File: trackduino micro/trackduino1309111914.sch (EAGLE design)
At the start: 35 parts, among them IC1 74AHC1G125DBV, IC2 74AHC1G125DBV, IC3 74AHC1G125DBV, U1 ATMEGA168

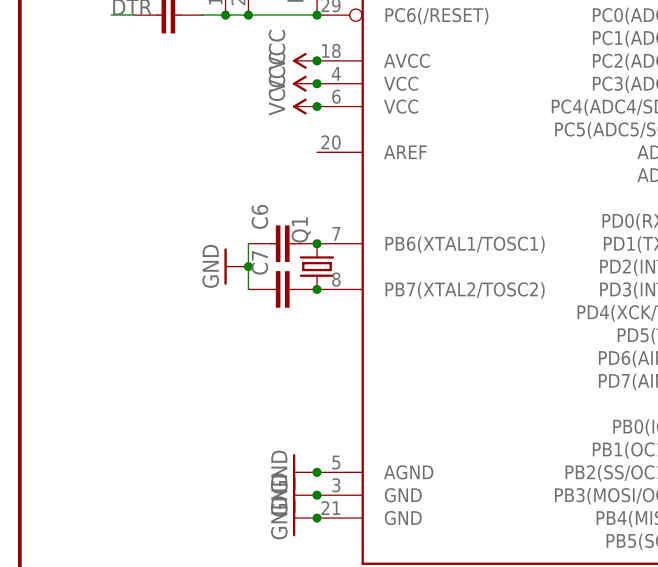
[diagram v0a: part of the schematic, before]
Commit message: swapped crystal for smaller resonator
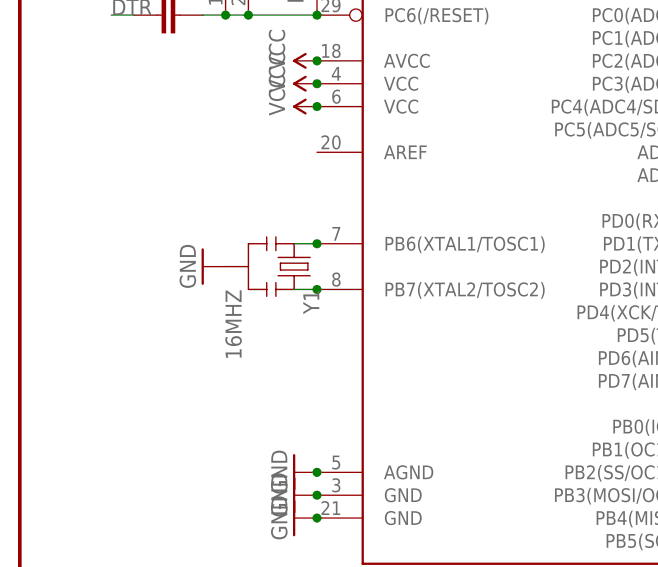
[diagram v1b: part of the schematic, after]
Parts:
- removed C6, C7: (no value), SparkFun-Capacitors:CAP0805
- removed Q1: (no value), crystal:CRYSTALCTS406
- added Y1: 16MHZ, SparkFun-FreqCtrl:RESONATOR16MHZ
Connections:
- net GND: now also Y1.2; no longer C6.1, C7.1
- net N$14: now also U1.PB7(XTAL2/TOSC2), Y1.3; no longer C6.2, Q1.2, U1.PB6(XTAL1/TOSC1)
- net N$26: now also U1.PB6(XTAL1/TOSC1), Y1.1; no longer C7.2, Q1.1, U1.PB7(XTAL2/TOSC2)
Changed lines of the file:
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@@
 <part name="S1" library="SparkFun-Electromechanical" deviceset="TAC_SWITCH" device="SMD" value="TAC_SWITCHSMD"/>
 <part name="GND23" library="SparkFun-Aesthetics" deviceset="GND" device=""/>
-<part name="Q1" library="crystal" deviceset="CRYSTAL" device="CTS406"/>
-<part name="C6" library="SparkFun-Capacitors" deviceset="CAP" device="0805"/>
-<part name="C7" library="SparkFun-Capacitors" deviceset="CAP" device="0805"/>
-<part name="GND24" library="SparkFun-Aesthetics" deviceset="GND" device=""/>
 <part name="FRAME1" library="SparkFun-Aesthetics" deviceset="FRAME-LETTER" device=""/>
 <part name="SUPPLY11" library="SparkFun-Aesthetics" deviceset="VCC" device=""/>
@@
 <part name="R6" library="SparkFun-Resistors" deviceset="RESISTOR" device="0805-RES"/>
 <part name="GND26" library="SparkFun-Aesthetics" deviceset="GND" device=""/>
+<part name="GND24" library="SparkFun-Aesthetics" deviceset="GND" device=""/>
+<part name="Y1" library="SparkFun-FreqCtrl" deviceset="RESONATOR" device="16MHZ" value="16MHZ"/>
 </parts>
 <sheets>
@@
 <instance part="S1" gate="S" x="22.86" y="86.36" rot="R90"/>
 <instance part="GND23" gate="1" x="27.94" y="91.44" rot="R90"/>
-<instance part="Q1" gate="G$1" x="33.02" y="53.34" rot="R90"/>
-<instance part="C6" gate="G$1" x="30.48" y="55.88" rot="R90"/>
-<instance part="C7" gate="G$1" x="30.48" y="50.8" rot="R90"/>
-<instance part="GND24" gate="1" x="22.86" y="53.34" rot="R270"/>
 <instance part="FRAME1" gate="G$1" x="0" y="0"/>
 <instance part="FRAME1" gate="G$2" x="147.32" y="0"/>
@@
 <instance part="R6" gate="G$1" x="154.94" y="68.58" rot="R270"/>
 <instance part="GND26" gate="1" x="154.94" y="83.82" rot="R180"/>
+<instance part="GND24" gate="1" x="20.32" y="53.34" rot="R270"/>
+<instance part="Y1" gate="G$1" x="30.48" y="53.34" rot="R270"/>
 </instances>
 <busses>
@@
 </segment>
 <segment>
-<pinref part="C6" gate="G$1" pin="1"/>
-<pinref part="C7" gate="G$1" pin="1"/>
-<wire x1="25.4" y1="55.88" x2="25.4" y2="53.34" width="0.1524" layer="91"/>
-<pinref part="GND24" gate="1" pin="GND"/>
-<wire x1="25.4" y1="53.34" x2="25.4" y2="50.8" width="0.1524" layer="91"/>
-<junction x="25.4" y="53.34"/>
-</segment>
-<segment>
 <pinref part="U1" gate="G$1" pin="AGND"/>
 <pinref part="GND25" gate="1" pin="GND"/>
@@
 <pinref part="GND26" gate="1" pin="GND"/>
 <junction x="154.94" y="81.28"/>
+</segment>
+<segment>
+<pinref part="GND24" gate="1" pin="GND"/>
+<pinref part="Y1" gate="G$1" pin="2"/>
 </segment>
 </net>
@@
 </segment>
 </net>
-<net name="N$14" class="0">
-<segment>
-<pinref part="U1" gate="G$1" pin="PB6(XTAL1/TOSC1)"/>
-<pinref part="Q1" gate="G$1" pin="2"/>
-<pinref part="C6" gate="G$1" pin="2"/>
-<junction x="33.02" y="55.88"/>
-<pinref part="C6" gate="G$1" pin="2"/>
-</segment>
-</net>
-<net name="N$26" class="0">
-<segment>
-<pinref part="U1" gate="G$1" pin="PB7(XTAL2/TOSC2)"/>
-<pinref part="Q1" gate="G$1" pin="1"/>
-<pinref part="C7" gate="G$1" pin="2"/>
-<junction x="33.02" y="50.8"/>
-<pinref part="C7" gate="G$1" pin="2"/>
-</segment>
-</net>
 <net name="N$27" class="0">
 <segment>
@@
 </segment>
 </net>
+<net name="N$14" class="0">
+<segment>
+<pinref part="U1" gate="G$1" pin="PB7(XTAL2/TOSC2)"/>
+<wire x1="30.48" y1="50.8" x2="33.02" y2="50.8" width="0.1524" layer="91"/>
+<junction x="33.02" y="50.8"/>
+<pinref part="Y1" gate="G$1" pin="3"/>
+</segment>
+</net>
+<net name="N$26" class="0">
+<segment>
+<pinref part="U1" gate="G$1" pin="PB6(XTAL1/TOSC1)"/>
+<wire x1="30.48" y1="55.88" x2="33.02" y2="55.88" width="0.1524" layer="91"/>
+<junction x="33.02" y="55.88"/>
+<pinref part="Y1" gate="G$1" pin="1"/>
+</segment>
+</net>
